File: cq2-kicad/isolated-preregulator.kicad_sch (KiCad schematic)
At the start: 43 parts, among them Q4 XPH4R10, Q5 XPH4R10, Q6 XPH4R10, Q7 XPH4R10, T1 378 uH, U42 LM5046MH, U63 100 %

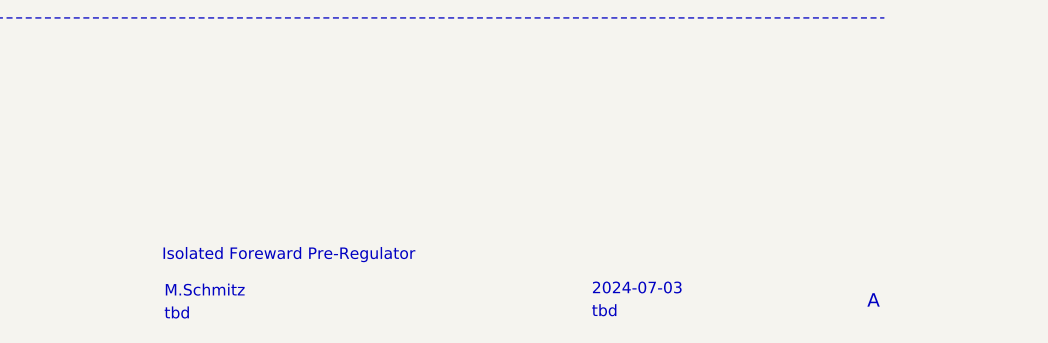
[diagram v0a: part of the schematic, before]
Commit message: drc checked before panalization
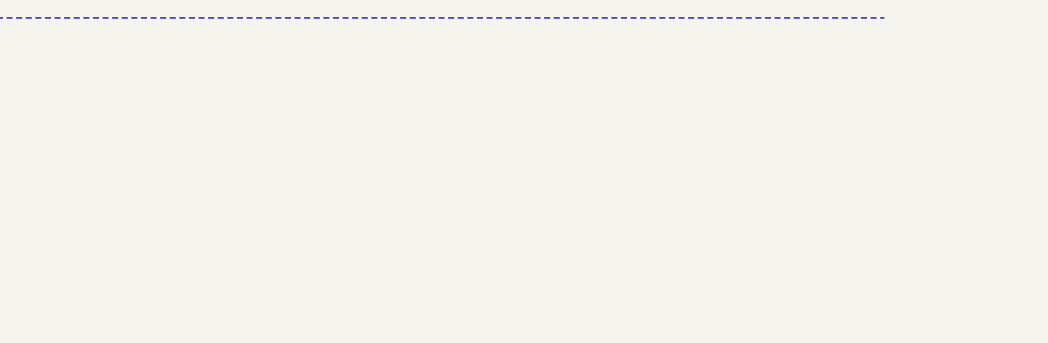
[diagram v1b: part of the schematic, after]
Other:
- note removed: "2024-07-03"
- note removed: "A"
- note removed: "Isolated Foreward Pre-Regulator"
- note removed: "M.Schmitz"
- note removed: "tbd"
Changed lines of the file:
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@@
 	(title_block
 		(title "CQ2")
-		(date "2024-07-17")
+		(date "2024-07-31")
 		(rev "0")
+		(comment 1 "Isolated Foreward Pre-Regulator")
+		(comment 2 "Manfred Schmitz")
+		(comment 3 "tbd")
+		(comment 4 "2024-07-03")
+		(comment 5 "tbd")
+		(comment 6 "A")
 	)
 	(junction
@@
 			(width 0)
 			(type default)
-		)
-	)
-	(text "tbd"
-		(exclude_from_sim no)
-		(at 190.5 193.802 0)
-		(effects
-			(font
-				(size 1.27 1.27)
-			)
-			(justify left bottom)
-		)
-	)
-	(text "tbd"
-		(exclude_from_sim no)
-		(at 237.998 193.548 0)
-		(effects
-			(font
-				(size 1.27 1.27)
-			)
-			(justify left bottom)
-		)
-	)
-	(text "Isolated Foreward Pre-Regulator"
-		(exclude_from_sim no)
-		(at 190.246 187.198 0)
-		(effects
-			(font
-				(size 1.27 1.27)
-			)
-			(justify left bottom)
-		)
-	)
-	(text "2024-07-03"
-		(exclude_from_sim no)
-		(at 237.998 191.008 0)
-		(effects
-			(font
-				(size 1.27 1.27)
-			)
-			(justify left bottom)
 		)
 	)
@@
 		)
 	)
-	(text "A"
-		(exclude_from_sim no)
-		(at 268.605 192.532 0)
-		(effects
-			(font
-				(size 1.4986 1.4986)
-			)
-			(justify left bottom)
-		)
-	)
 	(text "Tap \n= Tpa\n= 45ns"
 		(exclude_from_sim no)
@@
 		)
 	)
-	(text "M.Schmitz"
-		(exclude_from_sim no)
-		(at 190.5 191.262 0)
-		(effects
-			(font
-				(size 1.27 1.27)
-			)
-			(justify left bottom)
-		)
-	)

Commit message: Production documents created
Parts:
- Q4, Q5, Q6, Q7: Outline (none) -> SMT SOP-Advance-8
- R260, R261: Value2 100 ppm -> (none); Value3 62.5 mW -> (none); Value4 50 V -> (none)
- T1: Lifecycle review pending CQ2 -> EPR1 pending CQ2; Outline SMZ 23.37x20.83x9.14mm -> SMT 23.37x20.83x9.14mm
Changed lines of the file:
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@@
 	(title_block
 		(title "CQ2")
-		(date "2024-07-31")
+		(date "2024-08-03")
 		(rev "0")
 		(comment 1 "Isolated Foreward Pre-Regulator")
@@
 			)
 		)
-		(property "Description" "Transistor MOSFET N-Channel - SMT"
+		(property "Description" "Transistor MOSFET N-Channel"
 			(at 198.12 72.39 0)
 			(effects
@@
 			)
 		)
-		(property "Outline" ""
+		(property "Outline" "SMT SOP-Advance-8"
 			(at 198.12 72.39 0)
 			(effects
@@
 			)
 		)
-		(property "Lifecycle" "review pending CQ2"
+		(property "Lifecycle" "EPR1 pending CQ2"
 			(at 124.46 156.21 0)
 			(effects
@@
 			)
 		)
-		(property "Outline" "SMZ 23.37x20.83x9.14mm"
+		(property "Outline" "SMT 23.37x20.83x9.14mm"
 			(at 124.46 156.21 0)
 			(effects
@@
 			)
 		)
-		(property "Description" "Transistor MOSFET N-Channel - SMT"
+		(property "Description" "Transistor MOSFET N-Channel"
 			(at 241.3 53.34 0)
 			(effects
@@
 			)
 		)
-		(property "Outline" ""
+		(property "Outline" "SMT SOP-Advance-8"
 			(at 241.3 53.34 0)
 			(effects
@@
 			)
 		)
-		(property "Description" "Transistor MOSFET N-Channel - SMT"
+		(property "Description" "Transistor MOSFET N-Channel"
 			(at 241.3 72.39 0)
 			(effects
@@
 			)
 		)
-		(property "Outline" ""
+		(property "Outline" "SMT SOP-Advance-8"
 			(at 241.3 72.39 0)
 			(effects
@@
 			)
 		)
-		(property "Value2" "100 ppm"
+		(property "Value2" ""
 			(at 195.58 63.5 0)
 			(effects
@@
 			)
 		)
-		(property "Value3" "62.5 mW"
+		(property "Value3" ""
 			(at 195.58 63.5 0)
 			(effects
@@
 			)
 		)
-		(property "Value4" "50 V"
+		(property "Value4" ""
 			(at 195.58 63.5 0)
 			(effects
@@
 			)
 		)
-		(property "Description" "Transistor MOSFET N-Channel - SMT"
+		(property "Description" "Transistor MOSFET N-Channel"
 			(at 198.12 53.34 0)
 			(effects
@@
 			)
 		)
-		(property "Outline" ""
+		(property "Outline" "SMT SOP-Advance-8"
 			(at 198.12 53.34 0)
 			(effects
@@
 			)
 		)
-		(property "Value2" "100 ppm"
+		(property "Value2" ""
 			(at 243.84 63.5 0)
 			(effects
@@
 			)
 		)
-		(property "Value3" "62.5 mW"
+		(property "Value3" ""
 			(at 243.84 63.5 0)
 			(effects
@@
 			)
 		)
-		(property "Value4" "50 V"
+		(property "Value4" ""
 			(at 243.84 63.5 0)
 			(effects

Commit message: cq2 adapter in work
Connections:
- net at Q7.4 (G): now also U42.16 (LO2); no longer U42.12 (LO2)
- net at C199.2, R261.2: now also U42.12 (HS2); no longer U42.16 (HS2)
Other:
- note added: "U44 Pin 12 und 16 vertauscht C180 100pF"
